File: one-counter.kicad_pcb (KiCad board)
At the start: 2 copper layers, 14 parts, among them U1 L7805, U2 555-L, U3 555-R, U4 74LS90-L, U5 74LS90-R, U6 7447-L, U7 7447-R, U8 5082-7650-L, U9 5082-7650-R

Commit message: board laid out except 10 tracks
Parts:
- moved U1 103.6 mm to (149.6, 90.9), turned to 270 degrees
- moved C2 52.2 mm to (152.0, 124.8), turned to 270 degrees
- moved R3 49.9 mm to (154.5, 88.1), turned to 90 degrees
- moved C1 49.1 mm to (159.5, 127.9)
- moved R1 48.0 mm to (153.7, 116.0), turned to 270 degrees
- moved U3 42.4 mm to (159.5, 115.8)
- moved R2 42.0 mm to (149.7, 117.8), turned to 270 degrees
- moved U2 39.6 mm to (159.1, 89.6)
- moved U4 26.4 mm to (166.3, 112.6)
- moved U5 26.1 mm to (166.3, 87.7)
- moved U6 12.7 mm to (171.3, 110.0)
- moved U7 12.3 mm to (171.2, 86.8)
- moved U8 2.75 mm to (176.4, 110.0)
- moved U9 1.27 mm to (174.8, 86.8)
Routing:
- net +5V: track 0.00 -> 66.8 mm
- net GND: track 0.00 -> 58.8 mm
- net Net-(R3-Pad2): track 0.00 -> 16.9 mm
- net Net-(U4-Pad1): track 0.00 -> 16.0 mm
- net Net-(C2-Pad1): track 0.00 -> 12.6 mm
- net /1Hz: track 0.00 -> 10.1 mm
- net Net-(R1-Pad2): track 0.00 -> 10.1 mm
- net Net-(U7-Pad12): track 0.00 -> 9.80 mm
- net Net-(U7-Pad14): track 0.00 -> 4.69 mm
- net Net-(U7-Pad11): track 0.00 -> 4.67 mm
- net Net-(C1-Pad1): track 0.00 -> 4.42 mm
- net Net-(U7-Pad10): track 0.00 -> 3.64 mm
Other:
- board outline added: 33.8 x 47.3 mm
- rule trace_min: 0.2 -> 0.1524
- rule via_min_drill: 0.3 -> 0.254
- rule via_min_size: 0.4 -> 0.381

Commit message: routing is possible
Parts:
- added J1: Conn_01x08-L, Pin_Headers:Pin_Header_Straight_1x08_Pitch2.54mm, F.Cu at (149.8, 115.1)
- added J2: Conn_01x08-R, Pin_Headers:Pin_Header_Straight_1x08_Pitch2.54mm, F.Cu at (149.9, 110.5)
- moved R3 34.7 mm to (168.7, 119.7)
- moved U7 30.6 mm to (171.4, 117.4)
- moved U9 30.6 mm to (175.1, 117.4)
- moved U6 23.2 mm to (170.7, 86.9)
- moved U8 23.2 mm to (175.8, 86.8)
- moved R1 6.28 mm to (153.3, 122.3)
- moved R2 6.28 mm to (149.3, 124.1)
- moved C1 6.28 mm to (159.1, 134.2)
- moved C2 6.28 mm to (151.6, 131.0)
- moved U4 6.28 mm to (165.9, 118.9)
- moved U3 6.28 mm to (159.1, 122.1)
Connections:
- C2 pad 1: Net-(C2-Pad1) -> U3-6
- R2 pad 2: Net-(C2-Pad1) -> U3-6
- U2 pad 2: Net-(C2-Pad1) -> U2-2
- U3 pad 6: Net-(C2-Pad1) -> U3-6
- U4 pad 1: Net-(U4-Pad1) -> U4-1
- U5 pad 12: Net-(U4-Pad1) -> U5-12
- U6 pad 7: Net-(U4-Pad1) -> U5-12
- U7 pad 13: Net-(U7-Pad13) -> U7-13
- U7 pad 15: Net-(U7-Pad15) -> U7-15
- U7 pad 9: Net-(U7-Pad9) -> U7-9
- U8 pad 1: Net-(U7-Pad13) -> U8-1
- U8 pad 2: Net-(U7-Pad15) -> U8-2
- U8 pad 7: Net-(U7-Pad9) -> U8-7
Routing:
- net GND: track 58.8 -> 97.7 mm
- net U5-12: track 0.00 -> 33.7 mm
- net U8-1: track 0.00 -> 32.8 mm, vias 0 -> 1
- net U8-2: track 0.00 -> 28.3 mm, vias 0 -> 1
- net U7-9: track 0.00 -> 25.9 mm, vias 0 -> 1
- net U3-6: track 0.00 -> 25.4 mm
- net +5V: track 66.8 -> 87.2 mm, vias 0 -> 1
- net U2-2: track 0.00 -> 19.7 mm
- net U8-7: track 0.00 -> 19.6 mm
- net Net-(U5-Pad9): track 0.00 -> 16.7 mm
- net Net-(U4-Pad1): track 16.0 -> 0.00 mm
- net U7-13: track 0.00 -> 15.4 mm
- net Net-(U5-Pad8): track 0.00 -> 15.4 mm
- net Net-(R3-Pad2): track 16.9 -> 4.16 mm
- net U4-1: track 0.00 -> 12.7 mm
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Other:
- board size 33.8 x 47.3 mm -> 33.8 x 53.7 mm

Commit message: don't need resistor
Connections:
- J1 pad 8: (no net) -> Net-(J1-Pad8)
- J2 pad 8: (no net) -> Net-(J2-Pad8)
- U1 pad 1: (no net) -> +VDC
- U4 pad 4: (no net) -> Net-(U4-Pad4)
- U5 pad 13: (no net) -> Net-(U5-Pad13)
- U6 pad 3: (no net) -> Net-(U6-Pad3)
- U6 pad 4: (no net) -> Net-(U6-Pad4)
- U6 pad 5: (no net) -> Net-(U6-Pad5)
- U7 pad 16: Net-(R3-Pad2) -> +5V
- U8 pad 4: (no net) -> Net-(U8-Pad4)
- U8 pad 5: (no net) -> Net-(U8-Pad5)
- U8 pad 6: (no net) -> Net-(U8-Pad6)
- U9 pad 12: (no net) -> Net-(U9-Pad12)
- U9 pad 9: (no net) -> Net-(U9-Pad9)
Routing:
- net +5V: track 87.2 -> 90.4 mm

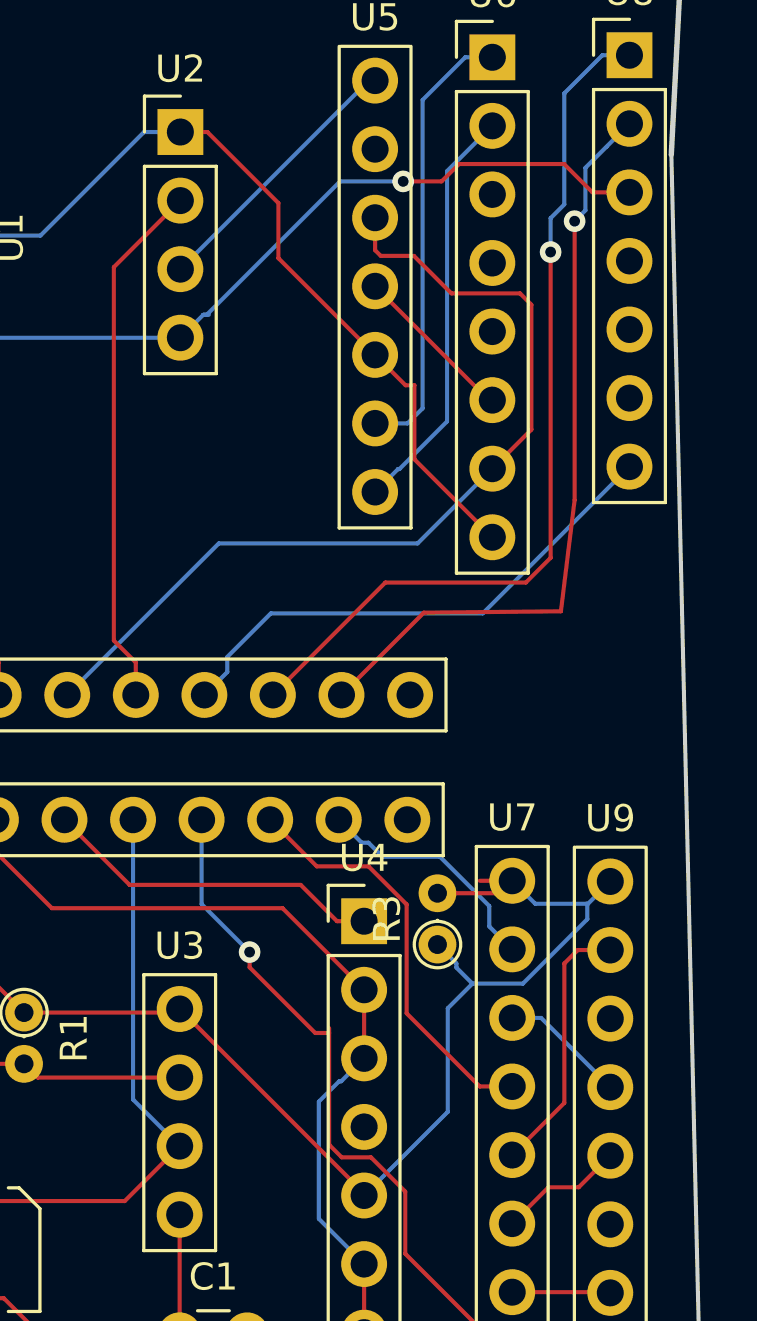
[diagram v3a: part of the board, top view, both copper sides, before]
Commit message: Run ERC/DRC and remove one anode connection
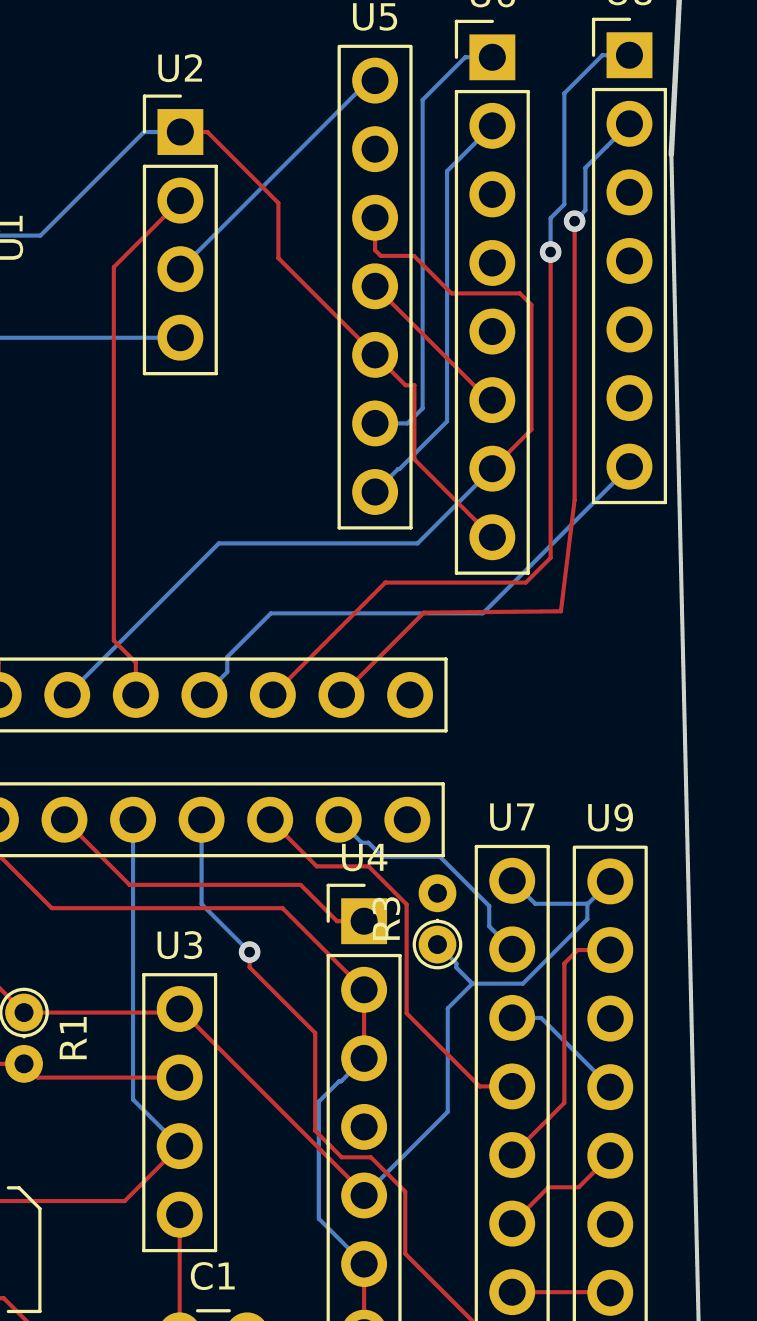
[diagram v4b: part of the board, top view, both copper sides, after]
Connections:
- U8 pad 3: +5V -> Net-(U8-Pad3)
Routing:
- net +5V: track 90.4 -> 70.4 mm, vias 1 -> 0
- net Net-(R3-Pad2): track 4.16 -> 0.00 mm
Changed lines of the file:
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@@
     (thickness 1.6)
     (drawings 7)
-    (tracks 176)
+    (tracks 162)
     (zones 0)
     (modules 16)
-    (nets 37)
+    (nets 38)
   )
   (page A4)
@@
   (net 35 "Net-(U9-Pad12)")
   (net 36 "Net-(U9-Pad9)")
+  (net 37 "Net-(U8-Pad3)")
   (net_class Default "This is the default net class."
     (clearance 0.2)
@@
     (add_net "Net-(U7-Pad12)")
     (add_net "Net-(U7-Pad14)")
+    (add_net "Net-(U8-Pad3)")
     (add_net "Net-(U8-Pad4)")
     (add_net "Net-(U8-Pad5)")
@@
       (net 21 U8-2))
     (pad 3 thru_hole oval (at 0 5.08) (size 1.7 1.7) (drill 1) (layers *.Cu *.Mask)
-      (net 3 +5V))
+      (net 37 "Net-(U8-Pad3)"))
     (pad 4 thru_hole oval (at 0 7.62) (size 1.7 1.7) (drill 1) (layers *.Cu *.Mask)
       (net 32 "Net-(U8-Pad4)"))
@@
   (segment (start 151.9682 95.8342) (end 149.606 93.472) (width 0.1524) (layer F.Cu) (net 2))
   (segment (start 151.9682 108.856119) (end 151.9682 95.8342) (width 0.1524) (layer F.Cu) (net 2))
-  (segment (start 159.980999 96.406601) (end 160.184199 96.406601) (width 0.1524) (layer B.Cu) (net 3))
-  (segment (start 159.131 97.2566) (end 159.980999 96.406601) (width 0.1524) (layer B.Cu) (net 3))
   (segment (start 174.206801 118.797977) (end 174.206801 118.248799) (width 0.1524) (layer B.Cu) (net 3))
   (segment (start 171.821378 121.1834) (end 174.206801 118.797977) (width 0.1524) (layer B.Cu) (net 3))
@@
   (segment (start 169.037 122.0978) (end 169.9514 121.1834) (width 0.1524) (layer B.Cu) (net 3))
   (segment (start 169.037 125.9332) (end 169.037 122.0978) (width 0.1524) (layer B.Cu) (net 3))
-  (segment (start 159.980999 96.406601) (end 160.107999 96.406601) (width 0.1524) (layer B.Cu) (net 3))
-  (via (at 167.386 91.4654) (size 0.8) (drill 0.4) (layers F.Cu B.Cu) (net 3))
-  (segment (start 160.107999 96.406601) (end 165.0492 91.4654) (width 0.1524) (layer B.Cu) (net 3))
-  (segment (start 165.0492 91.4654) (end 167.386 91.4654) (width 0.1524) (layer B.Cu) (net 3))
-  (segment (start 167.386 91.4654) (end 168.8084 91.4654) (width 0.1524) (layer F.Cu) (net 3))
-  (segment (start 169.452001 90.821799) (end 173.346399 90.821799) (width 0.1524) (layer F.Cu) (net 3))
-  (segment (start 168.8084 91.4654) (end 169.452001 90.821799) (width 0.1524) (layer F.Cu) (net 3))
-  (segment (start 174.3964 91.8718) (end 175.768 91.8718) (width 0.1524) (layer F.Cu) (net 3))
-  (segment (start 173.346399 90.821799) (end 174.3964 91.8718) (width 0.1524) (layer F.Cu) (net 3))
   (segment (start 149.86 96.266) (end 149.606 96.012) (width 0.1524) (layer F.Cu) (net 3))
   (segment (start 149.86 110.49) (end 149.86 96.266) (width 0.1524) (layer F.Cu) (net 3))
@@
   (segment (start 149.4028 124.1552) (end 149.3012 124.0536) (width 0.1524) (layer F.Cu) (net 4))
   (segment (start 153.3398 124.1552) (end 149.4028 124.1552) (width 0.1524) (layer F.Cu) (net 4))
-  (segment (start 171.4246 117.3734) (end 170.222519 117.3734) (width 0.1524) (layer F.Cu) (net 5))
-  (segment (start 170.9624 117.8356) (end 171.4246 117.3734) (width 0.1524) (layer F.Cu) (net 5))
-  (segment (start 168.656 117.8356) (end 170.9624 117.8356) (width 0.1524) (layer F.Cu) (net 5))
   (segment (start 166.116 87.7316) (end 166.3446 87.7316) (width 0.1524) (layer B.Cu) (net 6))
   (segment (start 159.131 94.7166) (end 166.116 87.7316) (width 0.1524) (layer B.Cu) (net 6))
@@
   (segment (start 167.4622 131.191) (end 167.4622 128.889222) (width 0.1524) (layer F.Cu) (net 18))
   (segment (start 167.4622 128.889222) (end 166.191179 127.618201) (width 0.1524) (layer F.Cu) (net 18))
-  (segment (start 165.108601 127.618201) (end 164.6428 127.1524) (width 0.1524) (layer F.Cu) (net 18))
   (via (at 161.6964 120.015) (size 0.8) (drill 0.4) (layers F.Cu B.Cu) (net 18))
   (segment (start 159.9184 115.1128) (end 159.9184 118.237) (width 0.1524) (layer B.Cu) (net 18))
   (segment (start 159.9184 118.237) (end 161.6964 120.015) (width 0.1524) (layer B.Cu) (net 18))
-  (segment (start 164.127915 123.0122) (end 164.6428 123.0122) (width 0.1524) (layer F.Cu) (net 18))
   (segment (start 161.6964 120.580685) (end 164.127915 123.0122) (width 0.1524) (layer F.Cu) (net 18))
   (segment (start 161.6964 120.015) (end 161.6964 120.580685) (width 0.1524) (layer F.Cu) (net 18))
-  (segment (start 164.6428 127.1524) (end 164.6428 123.0122) (width 0.1524) (layer F.Cu) (net 18))
-  (segment (start 164.6428 123.0122) (end 164.6428 122.8344) (width 0.1524) (layer F.Cu) (net 18))
+  (segment (start 164.127915 126.637515) (end 164.719 127.2286) (width 0.1524) (layer F.Cu) (net 18))
+  (segment (start 164.127915 123.0122) (end 164.127915 126.637515) (width 0.1524) (layer F.Cu) (net 18))
+  (segment (start 165.108601 127.618201) (end 164.719 127.2286) (width 0.1524) (layer F.Cu) (net 18))
+  (segment (start 164.719 127.2286) (end 164.6428 127.1524) (width 0.1524) (layer F.Cu) (net 18))
   (segment (start 170.222519 124.9934) (end 167.513 122.283881) (width 0.1524) (layer F.Cu) (net 19))
   (segment (start 171.4246 124.9934) (end 170.222519 124.9934) (width 0.1524) (layer F.Cu) (net 19))

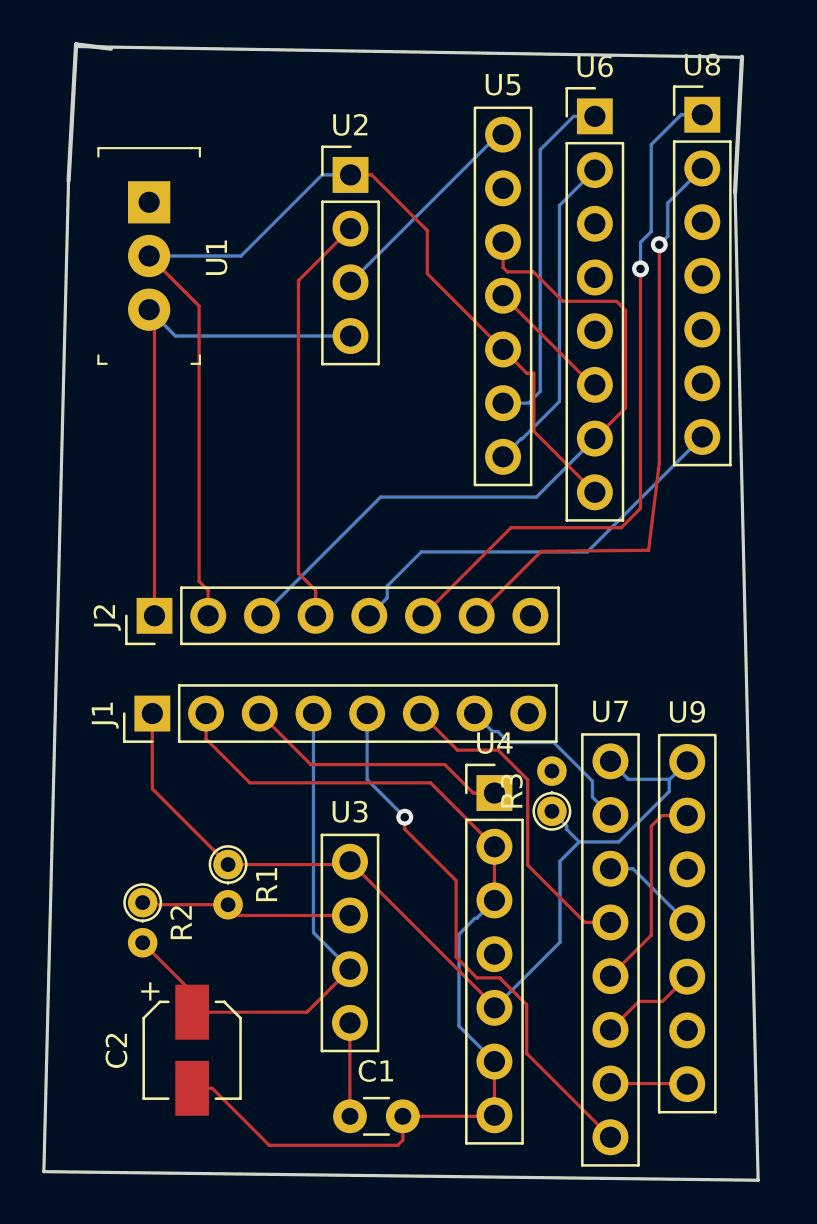
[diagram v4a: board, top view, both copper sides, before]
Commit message: move top components into place
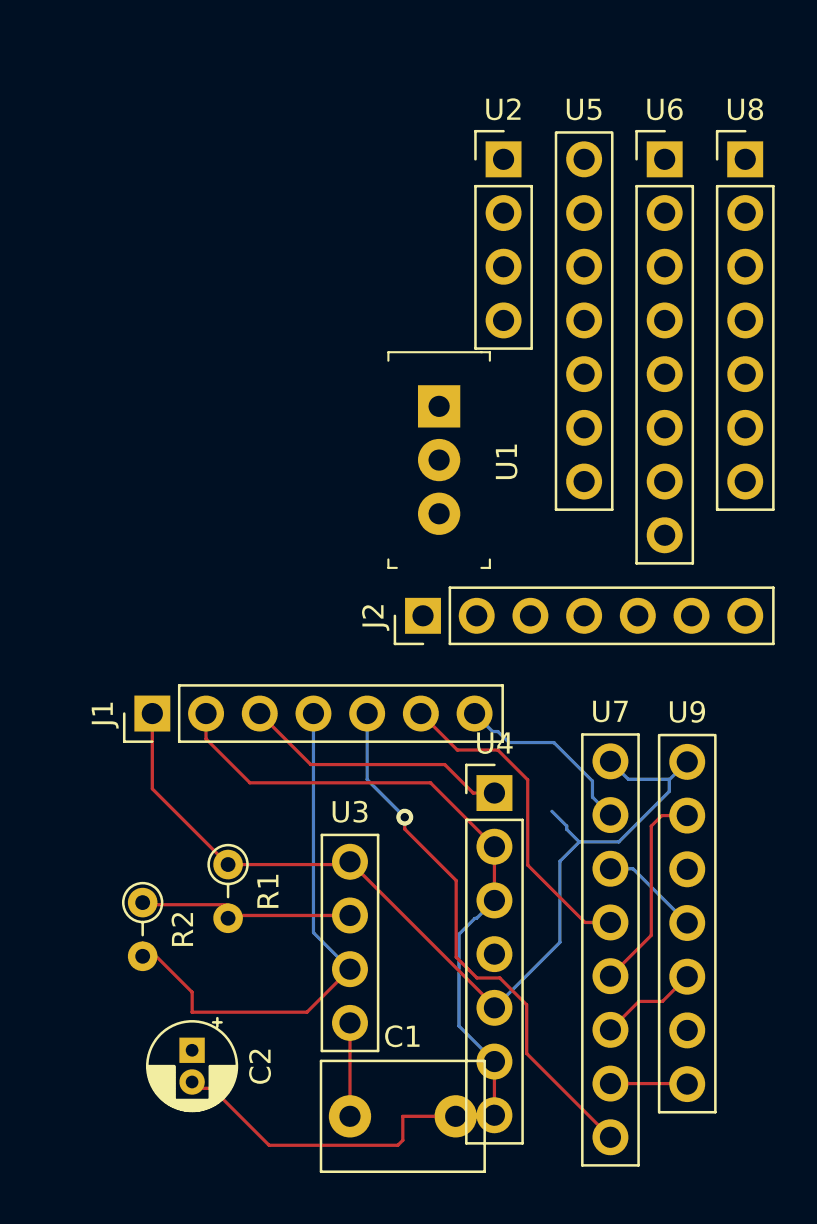
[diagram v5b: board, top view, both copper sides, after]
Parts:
- removed R3: 150, Resistors_THT:R_Axial_DIN0204_L3.6mm_D1.6mm_P1.90mm_Vertical
- C1: footprint Capacitors_THT:C_Disc_D3.0mm_W1.6mm_P2.50mm -> Capacitor_THT:C_Disc_D7.5mm_W5.0mm_P5.00mm
- C2: footprint Capacitors_SMD:CP_Elec_4x5.8 -> Capacitor_THT:CP_Radial_D4.0mm_P1.50mm
- J1: value Conn_01x08-L -> Conn_01x07-L; footprint Pin_Headers:Pin_Header_Straight_1x08_Pitch2.54mm -> Connector_PinHeader_2.54mm:PinHeader_1x07_P2.54mm_Vertical
- J2: value Conn_01x08-R -> Conn_01x07-R; footprint Pin_Headers:Pin_Header_Straight_1x08_Pitch2.54mm -> Connector_PinHeader_2.54mm:PinHeader_1x07_P2.54mm_Vertical
- R1, R2: footprint Resistors_THT:R_Axial_DIN0204_L3.6mm_D1.6mm_P1.90mm_Vertical -> Resistor_THT:R_Axial_DIN0204_L3.6mm_D1.6mm_P2.54mm_Vertical
- moved U1 16.8 mm to (163.3, 100.6)
- moved J2 12.7 mm to (162.6, 110.5)
- moved U2 7.28 mm to (166.4, 88.9)
- moved U5 4.01 mm to (170.2, 88.9)
- moved U6 3.88 mm to (174.0, 88.9)
- moved U8 2.93 mm to (177.8, 88.9)
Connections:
- U1 pad 1: +VDC -> (no net)
- U4 pad 4: Net-(U4-Pad4) -> (no net)
- U5 pad 13: Net-(U5-Pad13) -> (no net)
- U6 pad 3: Net-(U6-Pad3) -> (no net)
- U6 pad 4: Net-(U6-Pad4) -> (no net)
- U6 pad 5: Net-(U6-Pad5) -> (no net)
- U8 pad 3: Net-(U8-Pad3) -> (no net)
- U8 pad 4: Net-(U8-Pad4) -> (no net)
- U8 pad 5: Net-(U8-Pad5) -> (no net)
- U8 pad 6: Net-(U8-Pad6) -> (no net)
- U9 pad 12: Net-(U9-Pad12) -> (no net)
- U9 pad 9: Net-(U9-Pad9) -> (no net)
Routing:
- net GND: track 97.7 -> 47.8 mm
- net U5-12: track 33.7 -> 0.00 mm
- net U8-1: track 32.8 -> 0.00 mm, vias 1 -> 0
- net U8-2: track 28.3 -> 0.00 mm, vias 1 -> 0
- net +5V: track 70.4 -> 45.8 mm
- net U2-2: track 19.7 -> 0.00 mm
- net U8-7: track 19.6 -> 0.00 mm
- net Net-(U5-Pad9): track 16.7 -> 0.00 mm
- net Net-(U5-Pad8): track 15.4 -> 0.00 mm
- net /1Hz: track 10.1 -> 0.00 mm
- net Net-(U5-Pad11): track 6.09 -> 0.00 mm
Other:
- board outline removed
